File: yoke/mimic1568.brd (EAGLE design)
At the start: 165.1 x 114.3 mm, 23 parts, among them P1 1K, P2 1K, P3 44PINEDGE-M, U1 AD7533, U2 CD74HC573E, U3 CD74HCT75, U4 OPA2340N, U5 AD7533, U6 CD74HC573E

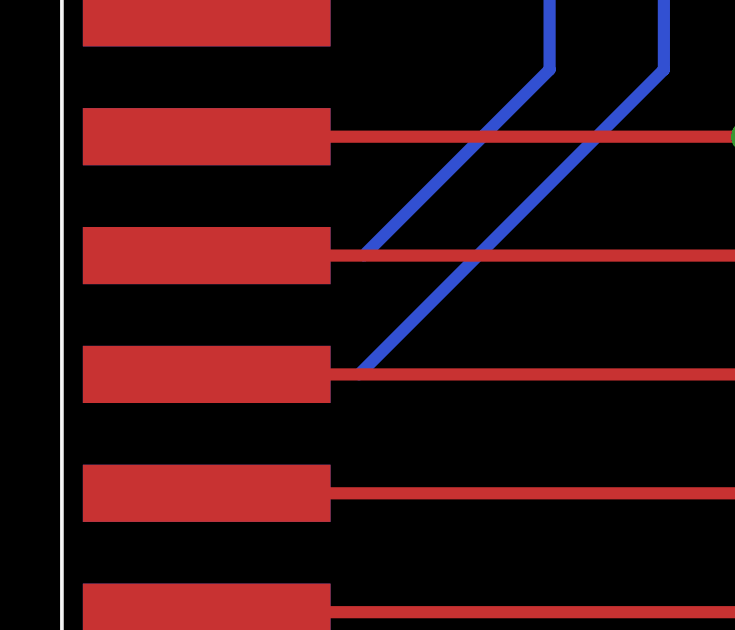
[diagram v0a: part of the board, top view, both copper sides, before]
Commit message: added missing connector on bckplane
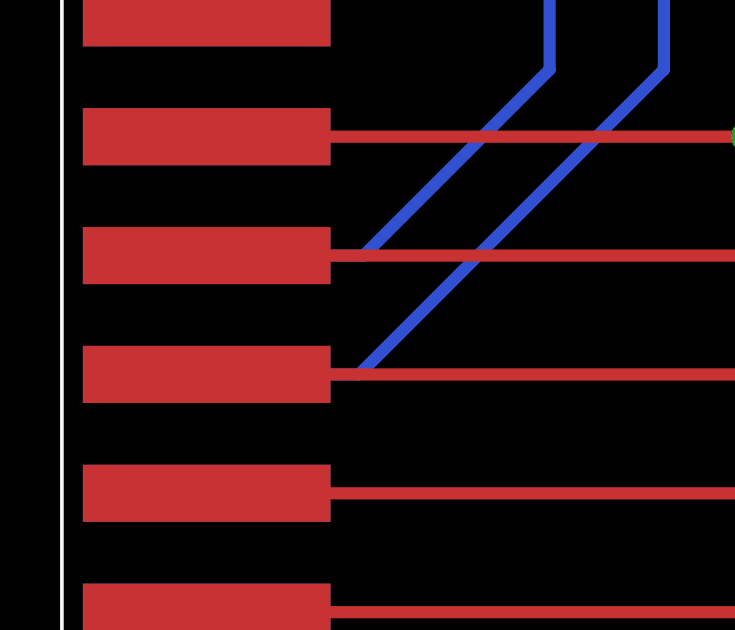
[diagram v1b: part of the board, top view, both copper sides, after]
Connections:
- removed net X_DAC: P3.J
- removed net Y_DAC: P3.K
- net XPOS: now also P3.J
- net YPOS: now also P3.K
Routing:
- net XPOS: track 24.6 -> 29.8 mm
- net YPOS: track 32.0 -> 37.0 mm
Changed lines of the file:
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@@
 <wire x1="20.066" y1="91.44" x2="20.066" y2="86.36" width="0.4064" layer="16"/>
 <wire x1="20.066" y1="86.36" x2="16.256" y2="82.55" width="0.4064" layer="16"/>
+<contactref element="P3" pad="J"/>
+<wire x1="4.826" y1="71.0184" x2="10.0584" y2="71.0184" width="0.4064" layer="16"/>
 </signal>
 <signal name="N$44">
@@
 <contactref element="R3" pad="1"/>
 <wire x1="28.194" y1="91.44" x2="20.066" y2="83.312" width="0.4064" layer="16"/>
+<contactref element="P3" pad="K"/>
+<wire x1="4.826" y1="67.056" x2="9.906" y2="67.056" width="0.4064" layer="16"/>
 </signal>
 <signal name="N$1">
@@
 <wire x1="117.856" y1="42.164" x2="117.856" y2="55.88" width="0.4064" layer="16"/>
 </signal>
-<signal name="X_DAC">
-<contactref element="P3" pad="J"/>
-</signal>
-<signal name="Y_DAC">
-<contactref element="P3" pad="K"/>
-</signal>
 </signals>
